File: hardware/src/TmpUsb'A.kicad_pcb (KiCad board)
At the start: 2 copper layers, 25 x 17 mm, 17 parts, among them P1 48037-2200, U1 PIC18F26J50

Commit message: Updated kicad PCB name
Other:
- board text added: "TmpUsb'A B"
- board text removed: "TmpUsb:A B"
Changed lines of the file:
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@@
   (gr_line (start 22 20) (end 41 20)
     (stroke (width 0.05) (type default)) (layer "Edge.Cuts"))
-  (gr_text "TmpUsb:A B" (at 42.352 36.238) (layer "B.SilkS")
+  (gr_text "TmpUsb'A B" (at 42.352 36.238) (layer "B.SilkS")
     (effects (font (size 1 1) (thickness 0.15)) (justify left bottom mirror))
   )

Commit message: Updated ICSP footprint
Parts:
- ?: footprint Medo64:ICSP PIC Pogo (6*w) -> Medo64:ICSP PIC Pogo (6w)
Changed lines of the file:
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@@
       (stroke (width 0.1) (type solid)) (fill solid) (layer "B.Mask"))
   )
-  (footprint "Medo64:ICSP PIC Pogo (6*w)" (layer "B.Cu")
+  (footprint "Medo64:ICSP PIC Pogo (6w)" (layer "B.Cu")
     (at 33.9 26.459 180)
     (attr smd)
-    (fp_text reference "" (at 0 1.37 unlocked) (layer "B.SilkS") hide
+    (fp_text reference "" (at 0 1.4 unlocked) (layer "B.SilkS") hide
         (effects (font (size 0.7 0.6) (thickness 0.1)) (justify bottom mirror))
     )
-    (fp_text value "J ICSP PIC Pogo (~{6}w)" (at 0 -1.47 unlocked) (layer "B.Fab") hide
+    (fp_text value "J ICSP PIC Pogo (~{6}w)" (at 0 -1.5 unlocked) (layer "B.Fab") hide
         (effects (font (size 0.7 0.6) (thickness 0.1) bold) (justify top mirror))
     )
+    (fp_text user "CLK" (at 3.81 1.07 unlocked) (layer "User.7")
+        (effects (font (size 0.13 0.07) (thickness 0.01)) (justify top))
+    )
     (fp_text user "Vpp" (at -6.35 1.07 unlocked) (layer "User.7")
+        (effects (font (size 0.13 0.07) (thickness 0.014) bold) (justify top))
+    )
+    (fp_text user "VPP" (at -6.35 1.07 unlocked) (layer "User.7")
         (effects (font (size 0.13 0.07) (thickness 0.014) bold) (justify top))
     )
@@
         (effects (font (size 0.13 0.07) (thickness 0.014) bold) (justify top))
     )
-    (fp_text user "PGC" (at 1.27 1.07 unlocked) (layer "User.7")
-        (effects (font (size 0.13 0.07) (thickness 0.01)) (justify top))
-    )
-    (fp_text user "PGD" (at 3.81 1.07 unlocked) (layer "User.7")
-        (effects (font (size 0.13 0.07) (thickness 0.01)) (justify top))
+    (fp_text user "VDD" (at -3.81 1.07 unlocked) (layer "User.7")
+        (effects (font (size 0.13 0.07) (thickness 0.014) bold) (justify top))
     )
     (fp_text user "Vdd" (at -3.81 1.07 unlocked) (layer "User.7")
         (effects (font (size 0.13 0.07) (thickness 0.014) bold) (justify top))
+    )
+    (fp_text user "DAT" (at 1.27 1.07 unlocked) (layer "User.7")
+        (effects (font (size 0.13 0.07) (thickness 0.01)) (justify top))
     )
     (fp_rect (start -7.62 1.27) (end 7.62 -1.27)
@@
     (pad "4" thru_hole circle (at 1.27 0 180) (size 1.4 1.4) (drill 0.9) (layers "*.Cu" "B.Mask")
       (net 13 "ICSP_PGD"))
-    (pad "5" thru_hole circle (at 3.81 0 180) (size 1.4 1.4) (drill 0.9) (layers "*.Cu" "B.Mask")
+    (pad "5" thru_hole circle (at 3.81 0 180) (size 1.4 1.4) (drill 0.9) (layers "*.Cu" "*.Mask")
       (net 14 "ICSP_PGC"))
   )

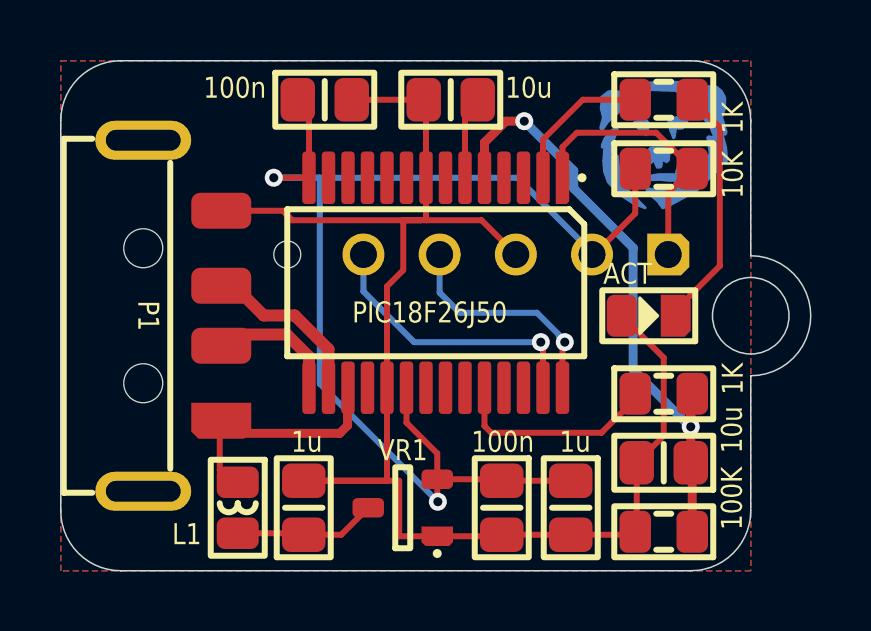
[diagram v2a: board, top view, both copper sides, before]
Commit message: Using 5-pin ICSP pogo connector
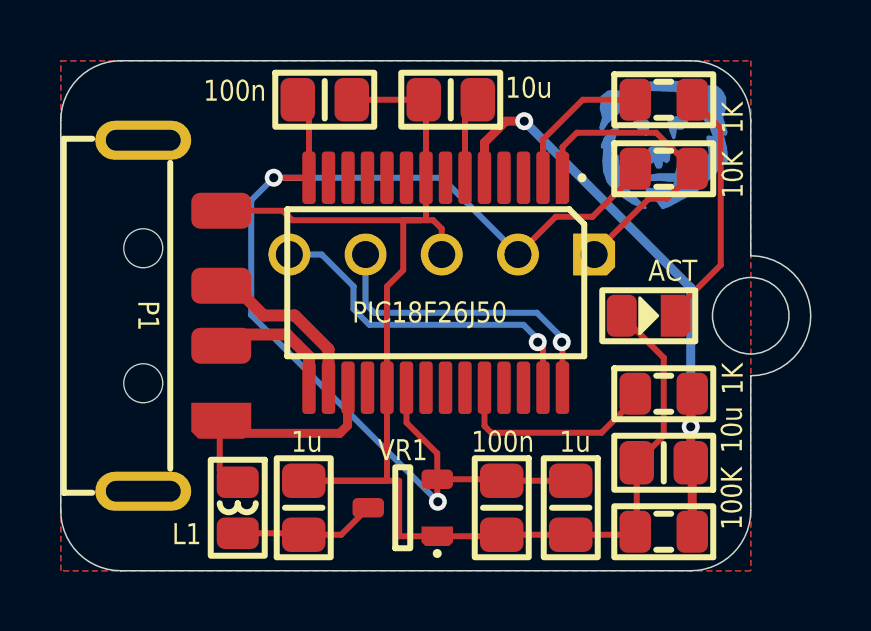
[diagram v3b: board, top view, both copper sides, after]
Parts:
- ?: footprint Medo64:ICSP PIC Pogo (6w) -> Medo64:ICSP PIC Pogo (5w)
- moved ? 1.20 mm to (32.7, 26.5)
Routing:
- net ICSP_PGD: track 7.71 -> 10.4 mm
- net ICSP_PGC: track 9.39 -> 11.6 mm
- net GND: track 49.5 -> 47.6 mm
- net ICSP_VPP: track 8.83 -> 10.0 mm
- net +3.3V: track 40.7 -> 39.5 mm

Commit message: Updated via size
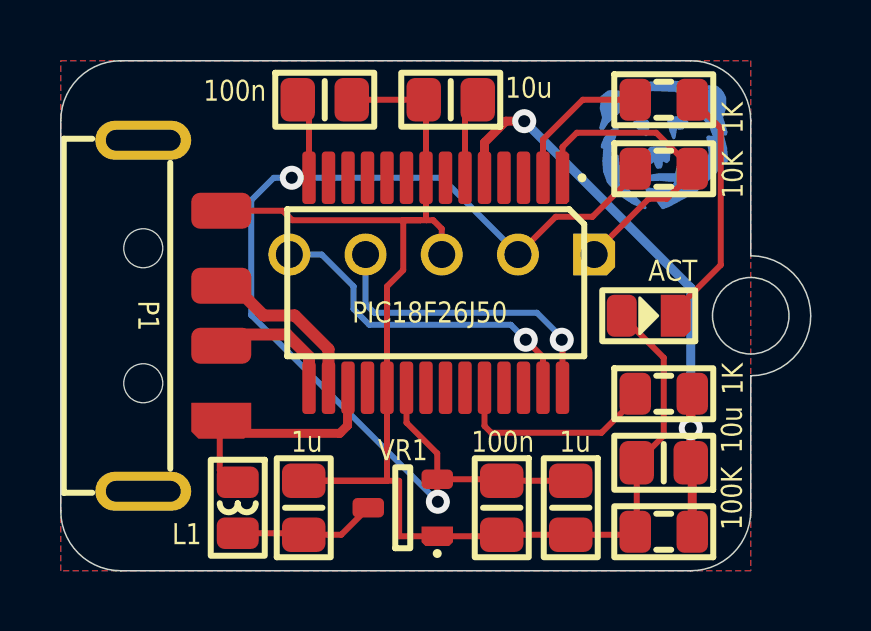
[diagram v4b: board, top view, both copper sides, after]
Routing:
- net +3.3V: track 39.5 -> 39.0 mm
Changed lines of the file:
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@@
   )
   (setup
+    (stackup
+      (layer "F.SilkS" (type "Top Silk Screen"))
+      (layer "F.Paste" (type "Top Solder Paste"))
+      (layer "F.Mask" (type "Top Solder Mask") (thickness 0.01))
+      (layer "F.Cu" (type "copper") (thickness 0.035))
+      (layer "dielectric 1" (type "core") (thickness 1.51) (material "FR4") (epsilon_r 4.5) (loss_tangent 0.02))
+      (layer "B.Cu" (type "copper") (thickness 0.035))
+      (layer "B.Mask" (type "Bottom Solder Mask") (thickness 0.01))
+      (layer "B.Paste" (type "Bottom Solder Paste"))
+      (layer "B.SilkS" (type "Bottom Silk Screen"))
+      (copper_finish "None")
+      (dielectric_constraints no)
+    )
     (pad_to_mask_clearance 0)
     (aux_axis_origin 20 37)
@@
   (segment (start 34.836 22.014) (end 34.125 22.725) (width 0.3) (layer "F.Cu") (net 4))
   (segment (start 35.45 22.014) (end 34.836 22.014) (width 0.3) (layer "F.Cu") (net 4))
-  (via (at 41 32.2) (size 0.6) (drill 0.3) (layers "F.Cu" "B.Cu") (net 4))
-  (via (at 35.45 22.014) (size 0.6) (drill 0.3) (layers "F.Cu" "B.Cu") (net 4))
+  (via (at 41 32.25) (size 0.8) (drill 0.4) (layers "F.Cu" "B.Cu") (net 4))
+  (via (at 35.45 22.014) (size 0.8) (drill 0.4) (layers "F.Cu" "B.Cu") (net 4))
   (segment (start 41 27.564) (end 41 32.2) (width 0.3) (layer "B.Cu") (net 4))
   (segment (start 35.45 22.014) (end 41 27.564) (width 0.3) (layer "B.Cu") (net 4))
@@
   (segment (start 31.525 32.065) (end 31.525 30.9) (width 0.2) (layer "F.Cu") (net 11))
   (segment (start 37.725 25.2) (end 36.499 25.2) (width 0.2) (layer "F.Cu") (net 11))
-  (segment (start 27.1 23.9) (end 28.275 23.9) (width 0.2) (layer "F.Cu") (net 11))
   (segment (start 39.15 23.775) (end 37.725 25.2) (width 0.2) (layer "F.Cu") (net 11))
   (segment (start 32.55 33.09) (end 31.525 32.065) (width 0.2) (layer "F.Cu") (net 11))
@@
   (segment (start 32.55 33.95) (end 32.55 34.68) (width 0.2) (layer "F.Cu") (net 11))
   (segment (start 32.55 33.95) (end 34.65 33.95) (width 0.2) (layer "F.Cu") (net 11))
+  (segment (start 27.6 23.9) (end 28.275 23.9) (width 0.25) (layer "F.Cu") (net 11))
   (segment (start 36.499 25.2) (end 35.24 26.459) (width 0.2) (layer "F.Cu") (net 11))
-  (via (at 32.57 34.7) (size 0.6) (drill 0.3) (layers "F.Cu" "B.Cu") (net 11))
-  (via (at 27.1 23.9) (size 0.6) (drill 0.3) (layers "F.Cu" "B.Cu") (net 11))
+  (via (at 32.57 34.7) (size 0.8) (drill 0.4) (layers "F.Cu" "B.Cu") (net 11))
+  (via (at 27.7 23.9) (size 0.8) (drill 0.4) (layers "F.Cu" "B.Cu") (net 11))
   (segment (start 32.57 34.7) (end 26.35 28.48) (width 0.2) (layer "B.Cu") (net 11))
   (segment (start 32.7 23.9) (end 35.24 26.44) (width 0.2) (layer "B.Cu") (net 11))
@@
   (segment (start 25.8 35.75) (end 28.05 35.75) (width 0.2) (layer "F.Cu") (net 12))
   (segment (start 28.1 35.8) (end 29.35 35.8) (width 0.2) (layer "F.Cu") (net 12))
-  (segment (start 36.801503 29.38) (end 36.725 29.456503) (width 0.2) (layer "F.Cu") (net 13))
   (segment (start 36.725 29.456503) (end 36.725 30.9) (width 0.2) (layer "F.Cu") (net 13))
-  (via (at 36.7 29.38) (size 0.6) (drill 0.3) (layers "F.Cu" "B.Cu") (net 13))
+  (via (at 36.7 29.3) (size 0.8) (drill 0.4) (layers "F.Cu" "B.Cu") (net 13))
   (segment (start 36.602 29.131471) (end 36.602 29.180497) (width 0.2) (layer "B.Cu") (net 13))
   (segment (start 35.870529 28.4) (end 36.602 29.131471) (width 0.2) (layer "B.Cu") (net 13))
@@
   (segment (start 30.16 28.11) (end 30.45 28.4) (width 0.2) (layer "B.Cu") (net 13))
   (segment (start 30.16 26.459) (end 30.16 28.11) (width 0.2) (layer "B.Cu") (net 13))
-  (segment (start 36.075 30.9) (end 36.075 29.453) (width 0.2) (layer "F.Cu") (net 14))
-  (segment (start 36.075 29.453) (end 36.002 29.38) (width 0.2) (layer "F.Cu") (net 14))
-  (via (at 35.9 29.38) (size 0.6) (drill 0.3) (layers "F.Cu" "B.Cu") (net 14))
+  (segment (start 36.075 29.875) (end 35.5 29.3) (width 0.2) (layer "F.Cu") (net 14))
+  (segment (start 36.075 30.9) (end 36.075 29.875) (width 0.2) (layer "F.Cu") (net 14))
+  (via (at 35.5 29.3) (size 0.8) (drill 0.4) (layers "F.Cu" "B.Cu") (net 14))
+  (segment (start 35 28.8) (end 30.284314 28.8) (width 0.2) (layer "B.Cu") (net 14))
   (segment (start 30.284314 28.8) (end 29.76 28.275685) (width 0.2) (layer "B.Cu") (net 14))
-  (segment (start 29.76 28.275685) (end 29.76 27.5195) (width 0.2) (layer "B.Cu") (net 14))
-  (segment (start 35.422 28.8) (end 30.284314 28.8) (width 0.2) (layer "B.Cu") (net 14))
+  (segment (start 35.58 29.38) (end 35 28.8) (width 0.2) (layer "B.Cu") (net 14))
   (segment (start 28.6995 26.459) (end 27.62 26.459) (width 0.2) (layer "B.Cu") (net 14))
   (segment (start 29.76 27.5195) (end 28.6995 26.459) (width 0.2) (layer "B.Cu") (net 14))
-  (segment (start 36.002 29.38) (end 35.422 28.8) (width 0.2) (layer "B.Cu") (net 14))
+  (segment (start 29.76 28.275685) (end 29.76 27.5195) (width 0.2) (layer "B.Cu") (net 14))
   (zone (net 3) (net_name "GND") (layers "F&B.Cu") (hatch none 0.5)
     (connect_pads (clearance 0.3))

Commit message: Updated pogo footprint
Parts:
- ?: footprint Medo64:ICSP PIC Pogo (5w) -> Medo64:ICSP PIC Pogo' (5w)
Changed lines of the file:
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@@
       (stroke (width 0.1) (type solid)) (fill solid) (layer "B.Mask"))
   )
-  (footprint "Medo64:ICSP PIC Pogo (5w)" (layer "B.Cu")
+  (footprint "Medo64:ICSP PIC Pogo' (5w)" (layer "B.Cu")
     (at 32.7 26.459 180)
     (attr smd)
@@
         (effects (font (size 0.7 0.6) (thickness 0.1) bold) (justify top mirror))
     )
+    (fp_text user "VPP" (at -5.08 1.07 unlocked) (layer "User.7")
+        (effects (font (size 0.13 0.07) (thickness 0.014) bold) (justify top))
+    )
     (fp_text user "Vpp" (at -6.35 1.07 unlocked) (layer "User.7")
         (effects (font (size 0.13 0.07) (thickness 0.014) bold) (justify top))
@@
         (effects (font (size 0.13 0.07) (thickness 0.014) bold) (justify top))
     )
+    (fp_text user "CLK" (at 5.08 1.07 unlocked) (layer "User.7")
+        (effects (font (size 0.13 0.07) (thickness 0.01)) (justify top))
+    )
     (fp_text user "GND" (at 0 1.07 unlocked) (layer "User.7")
         (effects (font (size 0.13 0.07) (thickness 0.014) bold) (justify top))
     )
-    (fp_text user "CLK" (at 5.08 1.07 unlocked) (layer "User.7")
-        (effects (font (size 0.13 0.07) (thickness 0.01)) (justify top))
-    )
     (fp_text user "DAT" (at 2.54 1.07 unlocked) (layer "User.7")
         (effects (font (size 0.13 0.07) (thickness 0.01)) (justify top))
-    )
-    (fp_text user "VPP" (at -5.08 1.07 unlocked) (layer "User.7")
-        (effects (font (size 0.13 0.07) (thickness 0.014) bold) (justify top))
     )
     (fp_text user "Vdd" (at -3.81 1.07 unlocked) (layer "User.7")
@@
     (fp_rect (start -6.35 1.27) (end 6.35 -1.27)
       (stroke (width 0.2) (type default)) (fill none) (layer "B.SilkS"))
+    (fp_poly
+      (pts
+        (xy -5.715 -1.27)
+        (xy -6.35 0)
+        (xy -6.35 -1.27)
+      )
+      (stroke (width 0) (type solid)) (fill solid) (layer "B.SilkS"))
+    (fp_poly
+      (pts
+        (xy -5.715 1.27)
+        (xy -6.35 1.27)
+        (xy -6.35 0)
+      )
+      (stroke (width 0) (type solid)) (fill solid) (layer "B.SilkS"))
     (pad "1" thru_hole roundrect (at -5.08 0 180) (size 1.4 1.4) (drill 0.9) (layers "*.Cu" "B.Mask") (roundrect_rratio 0.25)
       (chamfer_ratio 0.2) (chamfer top_left bottom_left)
